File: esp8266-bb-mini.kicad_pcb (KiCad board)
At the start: 2 copper layers, 34.3 x 31.8 mm, 20 parts, among them J1 Conn_01x02_Male, J2 Conn_01x04_Male, J3 Conn_01x04_Male, J4 Conn_01x04_Male, J5 Conn_01x04_Male, U1 LP38693MP-3.3, U2 ESP-12F

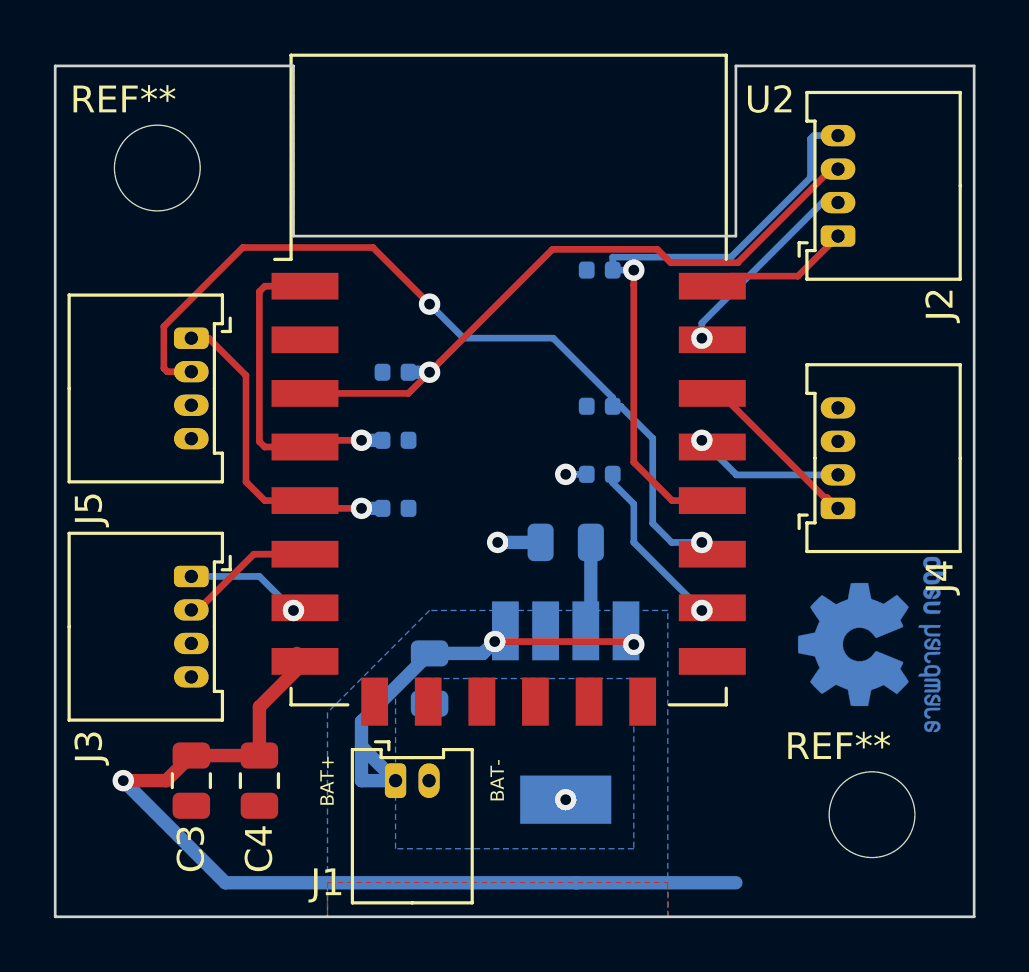
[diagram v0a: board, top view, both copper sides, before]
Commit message: brd: fix regression drd error
Signed-off-by: Tillmann Heidsieck <theidsieck@leenox.de>
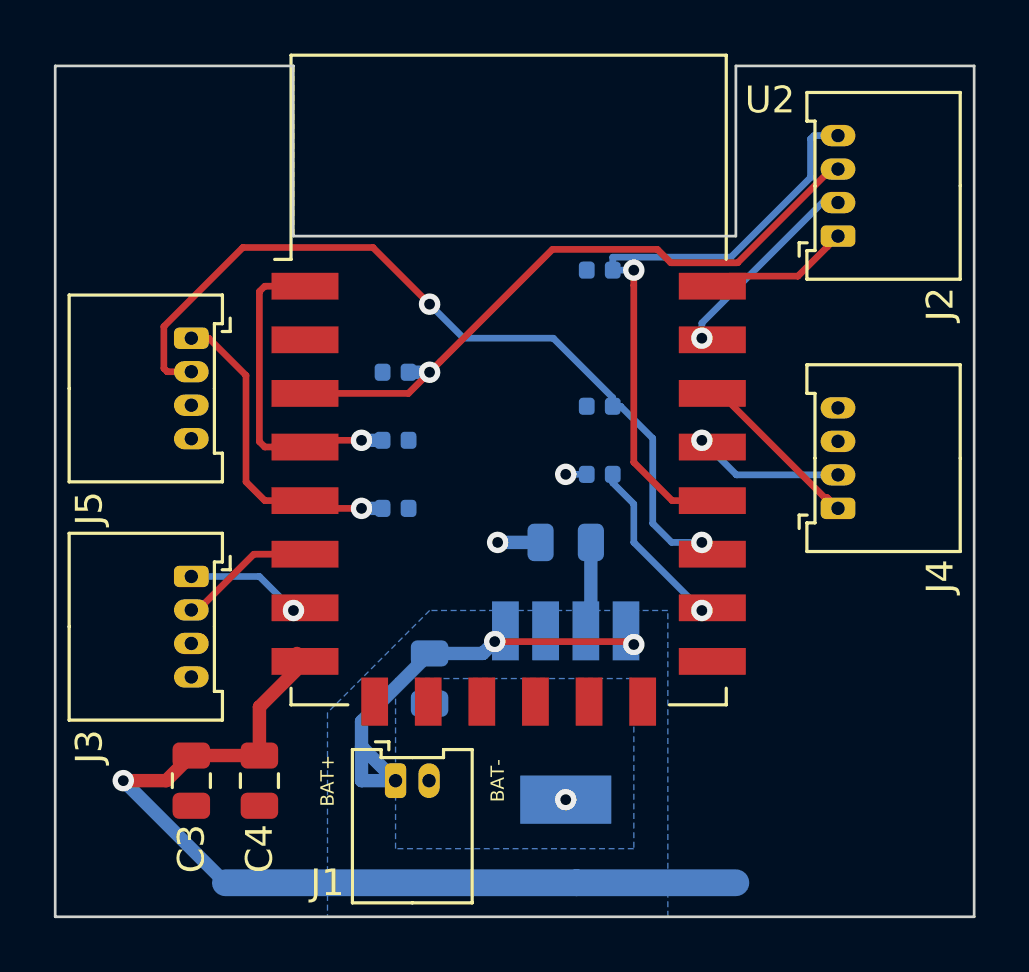
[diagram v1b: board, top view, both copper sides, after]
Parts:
- removed REF** (x2): MountingHole_3.2mm_M3, MountingHole:MountingHole_3.2mm_M3
- removed REF**: OSHW-Logo2_7.3x6mm_Copper, Symbol:OSHW-Logo2_7.3x6mm_Copper
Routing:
- removed copper zone on F.Cu, net +3V3
